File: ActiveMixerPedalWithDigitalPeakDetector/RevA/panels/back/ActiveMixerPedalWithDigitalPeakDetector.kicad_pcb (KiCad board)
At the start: 2 copper layers, 112.5 x 86.4 mm, 5 parts

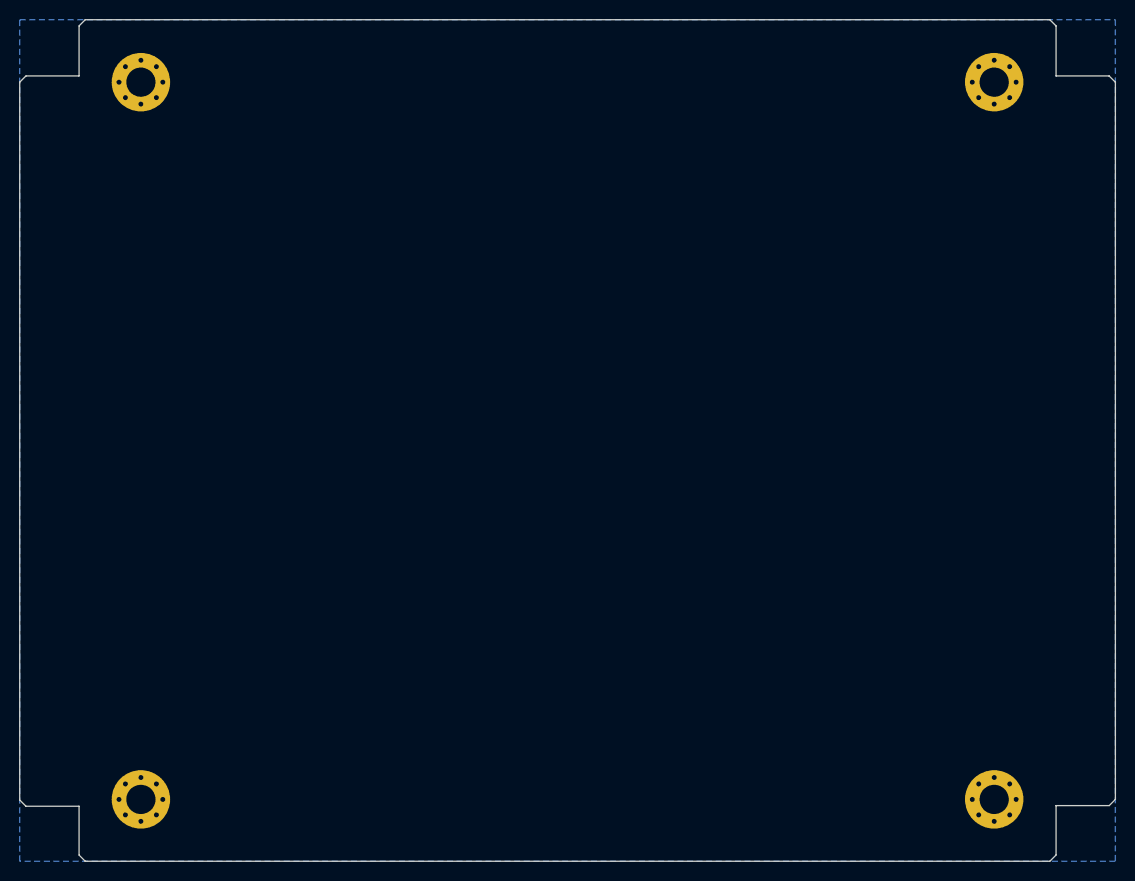
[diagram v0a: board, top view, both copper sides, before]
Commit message: updated front/back panel layout and gerbers
- Changed mount holes to non-via
- Changed BCu plane to FCu plane (same side as FCu silkscreen)
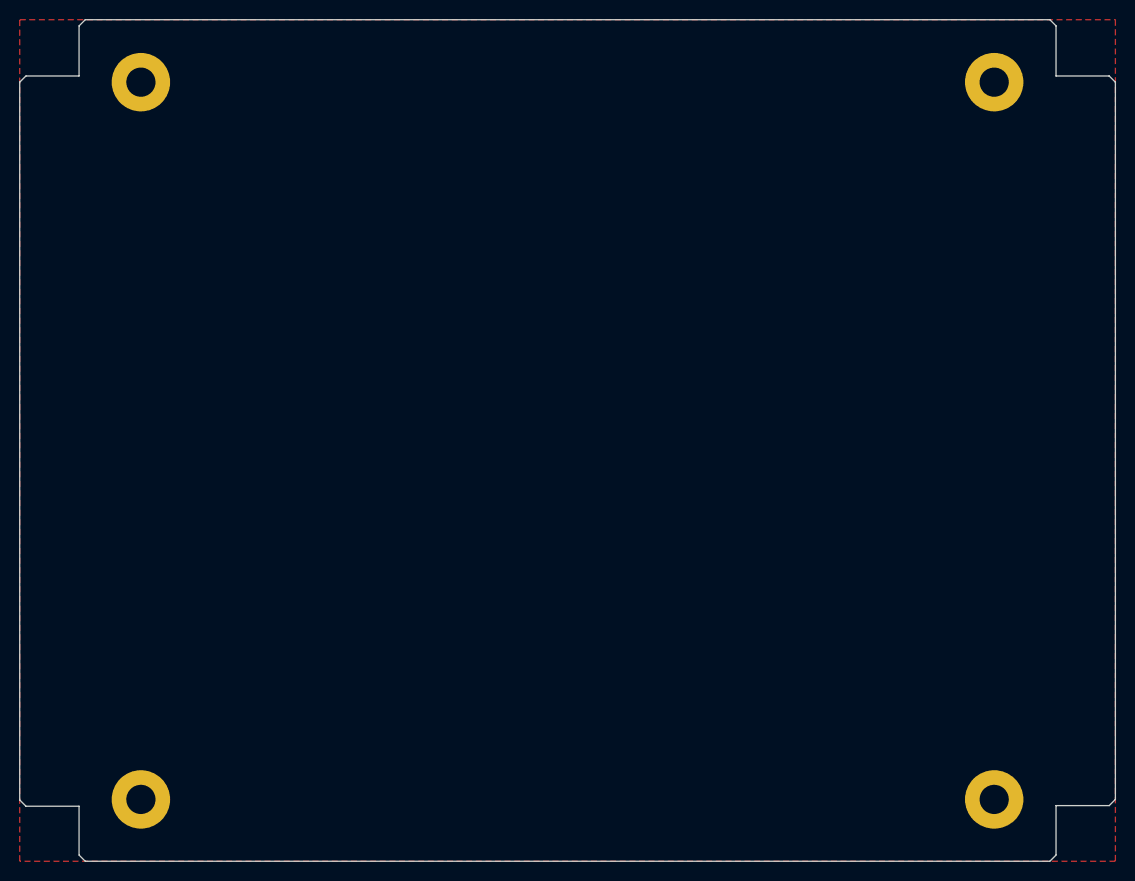
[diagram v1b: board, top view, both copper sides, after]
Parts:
- removed the REF** at (142.2, 134.6)
- removed the REF** at (54.6, 134.6)
- removed the REF** at (142.2, 61.0)
- added REF**: MountingHole_3mm_Pad, MountingHole:MountingHole_3mm_Pad, F.Cu at (54.6, 134.6)
- added REF**: MountingHole_3mm_Pad, MountingHole:MountingHole_3mm_Pad, F.Cu at (142.2, 61.0)
- added REF**: MountingHole_3mm_Pad, MountingHole:MountingHole_3mm_Pad, F.Cu at (142.2, 134.6)
- REF**: value MountingHole_3mm_Pad_Via -> MountingHole_3mm_Pad; footprint MountingHole:MountingHole_3mm_Pad_Via -> MountingHole:MountingHole_3mm_Pad
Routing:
- added copper zone on F.Cu, net (none)
- removed copper zone on B.Cu, net (none)
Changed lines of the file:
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@@
   (general
     (thickness 1.6)
-    (drawings 24)
+    (drawings 21)
     (tracks 0)
     (zones 0)
@@
     (diff_pair_gap 0.127)
   )
-  (module MountingHole:MountingHole_3mm_Pad_Via locked (layer F.Cu)
+  (module MountingHole:MountingHole_3mm_Pad locked (layer F.Cu)
+    (at 54.61 60.96)
+    (descr "Mounting Hole 3mm")
+    (tags "mounting hole 3mm")
+    (attr virtual)
+    (fp_text reference REF** (at 0 -4) (layer F.SilkS) hide
+      (effects (font (size 1 1) (thickness 0.15)))
+    )
+    (fp_text value MountingHole_3mm_Pad (at 0 4) (layer F.Fab)
+      (effects (font (size 1 1) (thickness 0.15)))
+    )
+    (fp_circle (center 0 0) (end 3.25 0) (layer F.CrtYd) (width 0.05))
+    (fp_circle (center 0 0) (end 3 0) (layer Cmts.User) (width 0.15))
+    (fp_text user %R (at 0.3 0) (layer F.Fab)
+      (effects (font (size 1 1) (thickness 0.15)))
+    )
+    (pad 1 thru_hole circle (at 0 0) (size 6 6) (drill 3) (layers *.Cu *.Mask))
+  )
+  (module MountingHole:MountingHole_3mm_Pad locked (layer F.Cu)
+    (at 54.61 134.62)
+    (descr "Mounting Hole 3mm")
+    (tags "mounting hole 3mm")
+    (attr virtual)
+    (fp_text reference REF** (at 0 -4) (layer F.SilkS) hide
+      (effects (font (size 1 1) (thickness 0.15)))
+    )
+    (fp_text value MountingHole_3mm_Pad (at 0 4) (layer F.Fab)
+      (effects (font (size 1 1) (thickness 0.15)))
+    )
+    (fp_circle (center 0 0) (end 3.25 0) (layer F.CrtYd) (width 0.05))
+    (fp_circle (center 0 0) (end 3 0) (layer Cmts.User) (width 0.15))
+    (fp_text user %R (at 0.3 0) (layer F.Fab)
+      (effects (font (size 1 1) (thickness 0.15)))
+    )
+    (pad 1 thru_hole circle (at 0 0) (size 6 6) (drill 3) (layers *.Cu *.Mask))
+  )
+  (module MountingHole:MountingHole_3mm_Pad locked (layer F.Cu)
+    (at 142.24 60.96)
+    (descr "Mounting Hole 3mm")
+    (tags "mounting hole 3mm")
+    (attr virtual)
+    (fp_text reference REF** (at 0 -4) (layer F.SilkS) hide
+      (effects (font (size 1 1) (thickness 0.15)))
+    )
+    (fp_text value MountingHole_3mm_Pad (at 0 4) (layer F.Fab)
+      (effects (font (size 1 1) (thickness 0.15)))
+    )
+    (fp_circle (center 0 0) (end 3.25 0) (layer F.CrtYd) (width 0.05))
+    (fp_circle (center 0 0) (end 3 0) (layer Cmts.User) (width 0.15))
+    (fp_text user %R (at 0.3 0) (layer F.Fab)
+      (effects (font (size 1 1) (thickness 0.15)))
+    )
+    (pad 1 thru_hole circle (at 0 0) (size 6 6) (drill 3) (layers *.Cu *.Mask))
+  )
+  (module MountingHole:MountingHole_3mm_Pad locked (layer F.Cu)
     (at 142.24 134.62)
     (descr "Mounting Hole 3mm")
@@
       (effects (font (size 1 1) (thickness 0.15)))
     )
-    (fp_text value MountingHole_3mm_Pad_Via (at 0 4) (layer F.Fab)
-      (effects (font (size 1 1) (thickness 0.15)))
-    )
-    (fp_circle (center 0 0) (end 3.25 0) (layer F.CrtYd) (width 0.05))
-    (fp_circle (center 0 0) (end 3 0) (layer Cmts.User) (width 0.15))
-    (fp_text user %R (at 0.3 0) (layer F.Fab)
-      (effects (font (size 1 1) (thickness 0.15)))
-    )
-    (pad 1 thru_hole circle (at 0 0) (size 6 6) (drill 3) (layers *.Cu *.Mask))
-    (pad 1 thru_hole circle (at 2.25 0) (size 0.8 0.8) (drill 0.5) (layers *.Cu *.Mask))
-    (pad 1 thru_hole circle (at 1.59099 1.59099) (size 0.8 0.8) (drill 0.5) (layers *.Cu *.Mask))
-    (pad 1 thru_hole circle (at 0 2.25) (size 0.8 0.8) (drill 0.5) (layers *.Cu *.Mask))
-    (pad 1 thru_hole circle (at -1.59099 1.59099) (size 0.8 0.8) (drill 0.5) (layers *.Cu *.Mask))
-    (pad 1 thru_hole circle (at -2.25 0) (size 0.8 0.8) (drill 0.5) (layers *.Cu *.Mask))
-    (pad 1 thru_hole circle (at -1.59099 -1.59099) (size 0.8 0.8) (drill 0.5) (layers *.Cu *.Mask))
-    (pad 1 thru_hole circle (at 0 -2.25) (size 0.8 0.8) (drill 0.5) (layers *.Cu *.Mask))
-    (pad 1 thru_hole circle (at 1.59099 -1.59099) (size 0.8 0.8) (drill 0.5) (layers *.Cu *.Mask))
-  )
-  (module MountingHole:MountingHole_3mm_Pad_Via locked (layer F.Cu)
-    (at 54.61 134.62)
-    (descr "Mounting Hole 3mm")
-    (tags "mounting hole 3mm")
-    (attr virtual)
-    (fp_text reference REF** (at 0 -4) (layer F.SilkS) hide
-      (effects (font (size 1 1) (thickness 0.15)))
-    )
-    (fp_text value MountingHole_3mm_Pad_Via (at 0 4) (layer F.Fab)
-      (effects (font (size 1 1) (thickness 0.15)))
-    )
-    (fp_circle (center 0 0) (end 3.25 0) (layer F.CrtYd) (width 0.05))
-    (fp_circle (center 0 0) (end 3 0) (layer Cmts.User) (width 0.15))
-    (fp_text user %R (at 0.3 0) (layer F.Fab)
-      (effects (font (size 1 1) (thickness 0.15)))
-    )
-    (pad 1 thru_hole circle (at 0 0) (size 6 6) (drill 3) (layers *.Cu *.Mask))
-    (pad 1 thru_hole circle (at 2.25 0) (size 0.8 0.8) (drill 0.5) (layers *.Cu *.Mask))
-    (pad 1 thru_hole circle (at 1.59099 1.59099) (size 0.8 0.8) (drill 0.5) (layers *.Cu *.Mask))
-    (pad 1 thru_hole circle (at 0 2.25) (size 0.8 0.8) (drill 0.5) (layers *.Cu *.Mask))
-    (pad 1 thru_hole circle (at -1.59099 1.59099) (size 0.8 0.8) (drill 0.5) (layers *.Cu *.Mask))
-    (pad 1 thru_hole circle (at -2.25 0) (size 0.8 0.8) (drill 0.5) (layers *.Cu *.Mask))
-    (pad 1 thru_hole circle (at -1.59099 -1.59099) (size 0.8 0.8) (drill 0.5) (layers *.Cu *.Mask))
-    (pad 1 thru_hole circle (at 0 -2.25) (size 0.8 0.8) (drill 0.5) (layers *.Cu *.Mask))
-    (pad 1 thru_hole circle (at 1.59099 -1.59099) (size 0.8 0.8) (drill 0.5) (layers *.Cu *.Mask))
-  )
-  (module MountingHole:MountingHole_3mm_Pad_Via locked (layer F.Cu)
-    (at 142.24 60.96)
-    (descr "Mounting Hole 3mm")
-    (tags "mounting hole 3mm")
-    (attr virtual)
-    (fp_text reference REF** (at 0 -4) (layer F.SilkS) hide
-      (effects (font (size 1 1) (thickness 0.15)))
-    )
-    (fp_text value MountingHole_3mm_Pad_Via (at 0 4) (layer F.Fab)
-      (effects (font (size 1 1) (thickness 0.15)))
-    )
-    (fp_circle (center 0 0) (end 3.25 0) (layer F.CrtYd) (width 0.05))
-    (fp_circle (center 0 0) (end 3 0) (layer Cmts.User) (width 0.15))
-    (fp_text user %R (at 0.3 0) (layer F.Fab)
-      (effects (font (size 1 1) (thickness 0.15)))
-    )
-    (pad 1 thru_hole circle (at 0 0) (size 6 6) (drill 3) (layers *.Cu *.Mask))
-    (pad 1 thru_hole circle (at 2.25 0) (size 0.8 0.8) (drill 0.5) (layers *.Cu *.Mask))
-    (pad 1 thru_hole circle (at 1.59099 1.59099) (size 0.8 0.8) (drill 0.5) (layers *.Cu *.Mask))
-    (pad 1 thru_hole circle (at 0 2.25) (size 0.8 0.8) (drill 0.5) (layers *.Cu *.Mask))
-    (pad 1 thru_hole circle (at -1.59099 1.59099) (size 0.8 0.8) (drill 0.5) (layers *.Cu *.Mask))
-    (pad 1 thru_hole circle (at -2.25 0) (size 0.8 0.8) (drill 0.5) (layers *.Cu *.Mask))
-    (pad 1 thru_hole circle (at -1.59099 -1.59099) (size 0.8 0.8) (drill 0.5) (layers *.Cu *.Mask))
-    (pad 1 thru_hole circle (at 0 -2.25) (size 0.8 0.8) (drill 0.5) (layers *.Cu *.Mask))
-    (pad 1 thru_hole circle (at 1.59099 -1.59099) (size 0.8 0.8) (drill 0.5) (layers *.Cu *.Mask))
-  )
-  (module MountingHole:MountingHole_3mm_Pad_Via locked (layer F.Cu)
-    (at 54.61 60.96)
-    (descr "Mounting Hole 3mm")
-    (tags "mounting hole 3mm")
-    (attr virtual)
-    (fp_text reference REF** (at 0 -4) (layer F.SilkS) hide
-      (effects (font (size 1 1) (thickness 0.15)))
-    )
-    (fp_text value MountingHole_3mm_Pad_Via (at 0 4) (layer F.Fab)
-      (effects (font (size 1 1) (thickness 0.15)))
-    )
-    (fp_circle (center 0 0) (end 3.25 0) (layer F.CrtYd) (width 0.05))
-    (fp_circle (center 0 0) (end 3 0) (layer Cmts.User) (width 0.15))
-    (fp_text user %R (at 0.3 0) (layer F.Fab)
-      (effects (font (size 1 1) (thickness 0.15)))
-    )
-    (pad 1 thru_hole circle (at 1.59099 -1.59099) (size 0.8 0.8) (drill 0.5) (layers *.Cu *.Mask))
-    (pad 1 thru_hole circle (at 0 -2.25) (size 0.8 0.8) (drill 0.5) (layers *.Cu *.Mask))
-    (pad 1 thru_hole circle (at -1.59099 -1.59099) (size 0.8 0.8) (drill 0.5) (layers *.Cu *.Mask))
-    (pad 1 thru_hole circle (at -2.25 0) (size 0.8 0.8) (drill 0.5) (layers *.Cu *.Mask))
-    (pad 1 thru_hole circle (at -1.59099 1.59099) (size 0.8 0.8) (drill 0.5) (layers *.Cu *.Mask))
-    (pad 1 thru_hole circle (at 0 2.25) (size 0.8 0.8) (drill 0.5) (layers *.Cu *.Mask))
-    (pad 1 thru_hole circle (at 1.59099 1.59099) (size 0.8 0.8) (drill 0.5) (layers *.Cu *.Mask))
-    (pad 1 thru_hole circle (at 2.25 0) (size 0.8 0.8) (drill 0.5) (layers *.Cu *.Mask))
+    (fp_text value MountingHole_3mm_Pad (at 0 4) (layer F.Fab)
+      (effects (font (size 1 1) (thickness 0.15)))
+    )
+    (fp_circle (center 0 0) (end 3.25 0) (layer F.CrtYd) (width 0.05))
+    (fp_circle (center 0 0) (end 3 0) (layer Cmts.User) (width 0.15))
+    (fp_text user %R (at 0.3 0) (layer F.Fab)
+      (effects (font (size 1 1) (thickness 0.15)))
+    )
     (pad 1 thru_hole circle (at 0 0) (size 6 6) (drill 3) (layers *.Cu *.Mask))
   )
@@
     (fp_line (start 43.2435 -49.53) (end 42.6085 -50.165) (layer Dwgs.User) (width 0.12))
   )
-  (gr_line (start -74.8665 46.9265) (end -76.6445 46.9265) (layer Dwgs.User) (width 0.15))
-  (gr_line (start -74.8665 40.64) (end -76.6445 40.64) (layer Dwgs.User) (width 0.15))
-  (gr_line (start -75.7555 40.64) (end -75.7555 46.9265) (layer Dwgs.User) (width 0.15))
   (gr_text -3V (at 54.102 137.6045) (layer B.SilkS)
     (effects (font (size 0.8 0.8) (thickness 0.15)) (justify mirror))
@@
   (gr_line (start 48.895 140.97) (end 48.26 140.335) (layer Edge.Cuts) (width 0.05))
   (gr_line (start 147.955 140.97) (end 48.895 140.97) (layer Edge.Cuts) (width 0.05))
-  (zone (net 0) (net_name "") (layer B.Cu) (hatch edge 0.508)
+  (zone (net 0) (net_name "") (layer F.Cu) (hatch edge 0.508)
     (connect_pads yes (clearance 0.508))
     (min_thickness 0.254)
